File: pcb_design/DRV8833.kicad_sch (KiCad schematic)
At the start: 7 parts, among them M1 motor, M2 motor, U3 DRV8833PW

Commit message: Correct BoM and placement files
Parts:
- R25: value 47k -> 4.7k
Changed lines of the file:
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@@
       (effects (font (size 1.27 1.27)) (justify right))
     )
-    (property "Value" "47k" (id 1) (at 132.334 85.598 90)
+    (property "Value" "4.7k" (id 1) (at 132.334 85.598 90)
       (effects (font (size 1.27 1.27)) (justify right))
     )

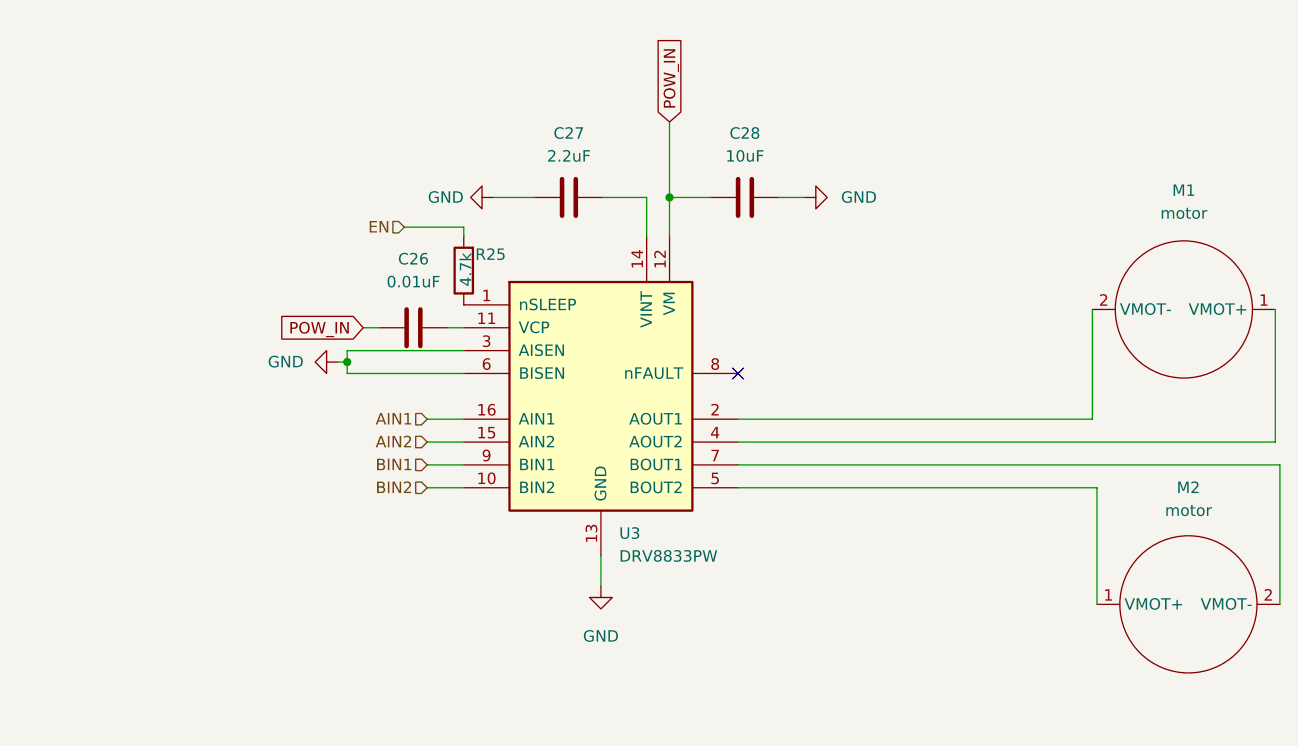
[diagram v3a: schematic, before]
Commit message: Updated PCB with HTSSOP16 package for DRV8833
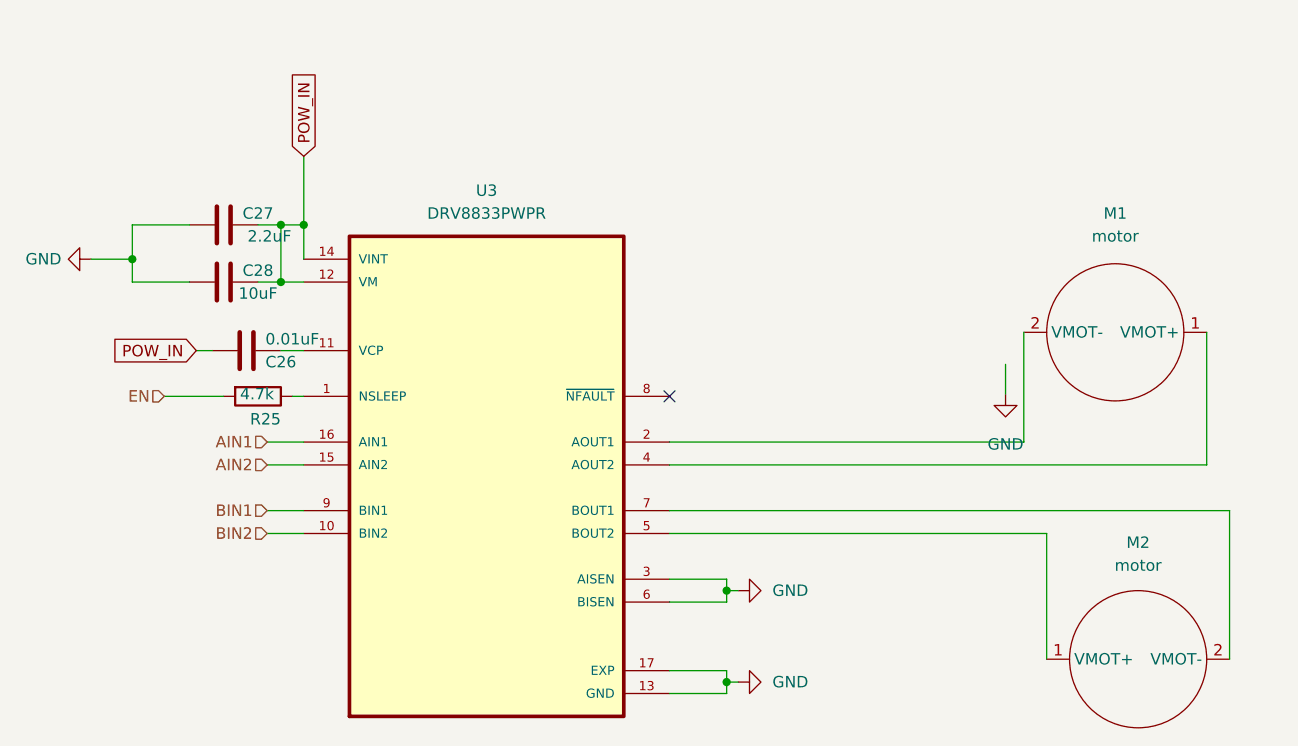
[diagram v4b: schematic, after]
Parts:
- removed U3: DRV8833PW, Package_SO:TSSOP-16_4.4x5mm_P0.65mm, symbol Driver_Motor:DRV8833PW
- added U3: DRV8833PWPR, IC_DRV8833PWPR, symbol DRV8833PWPR:DRV8833PWPR
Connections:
- net AIN1: now also U3.16 (AIN1)
- net AIN2: now also U3.15 (AIN2)
- net BIN1: now also U3.9 (BIN1)
- net BIN2: now also U3.10 (BIN2)
- net GND: now also C28.1, U3.13 (GND), U3.17 (EXP), U3.3 (AISEN), U3.6 (BISEN); no longer C28.2
- net POW_IN: now also C27.2, C28.2, U3.12 (VM), U3.14 (VINT); no longer C28.1
- net at R25.1: now also U3.1 (NSLEEP)
- net at M1.1 (VMOT+): now also U3.4 (AOUT2)
- net at M1.2 (VMOT-): now also U3.2 (AOUT1)
- net at C26.2: now also U3.11 (VCP)
- net at M2.1 (VMOT+): now also U3.5 (BOUT2)
- net at M2.2 (VMOT-): now also U3.7 (BOUT1)
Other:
- moved on the sheet: C26, C27, C28, M1, M2, R25

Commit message: Update Mushak PCB design to include new features (#5)
* Update mushak PCB with new changes
* Add AMS1117 as 3.3v regulator
* Add new alternate placement for IR sensors
* Add new 3.3v compatible ToF sensor
* Update gerber files

* Add changes to silkscreen and filter capacitors
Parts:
- U3: footprint IC_DRV8833PWPR -> DRV8833PWPR:IC_DRV8833PWPR
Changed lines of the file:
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@@
     (property "Reference" "U3" (id 0) (at 134.62 74.93 0))
     (property "Value" "DRV8833PWPR" (id 1) (at 134.62 77.47 0))
-    (property "Footprint" "IC_DRV8833PWPR" (id 2) (at 134.62 107.95 0)
+    (property "Footprint" "DRV8833PWPR:IC_DRV8833PWPR" (id 2) (at 134.62 107.95 0)
       (effects (font (size 1.27 1.27)) (justify left bottom) hide)
     )
